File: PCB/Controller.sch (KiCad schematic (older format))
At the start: 15 parts, among them IC501 ATMEGA88-A, P501 PRG, SW501 Time Set, SW502 Alarm Set, SW503 Fast, SW504 Slow, SW505 Auto Time, SW506 Sleep, SW507 Summer Time, SW508 Alarm Enabled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

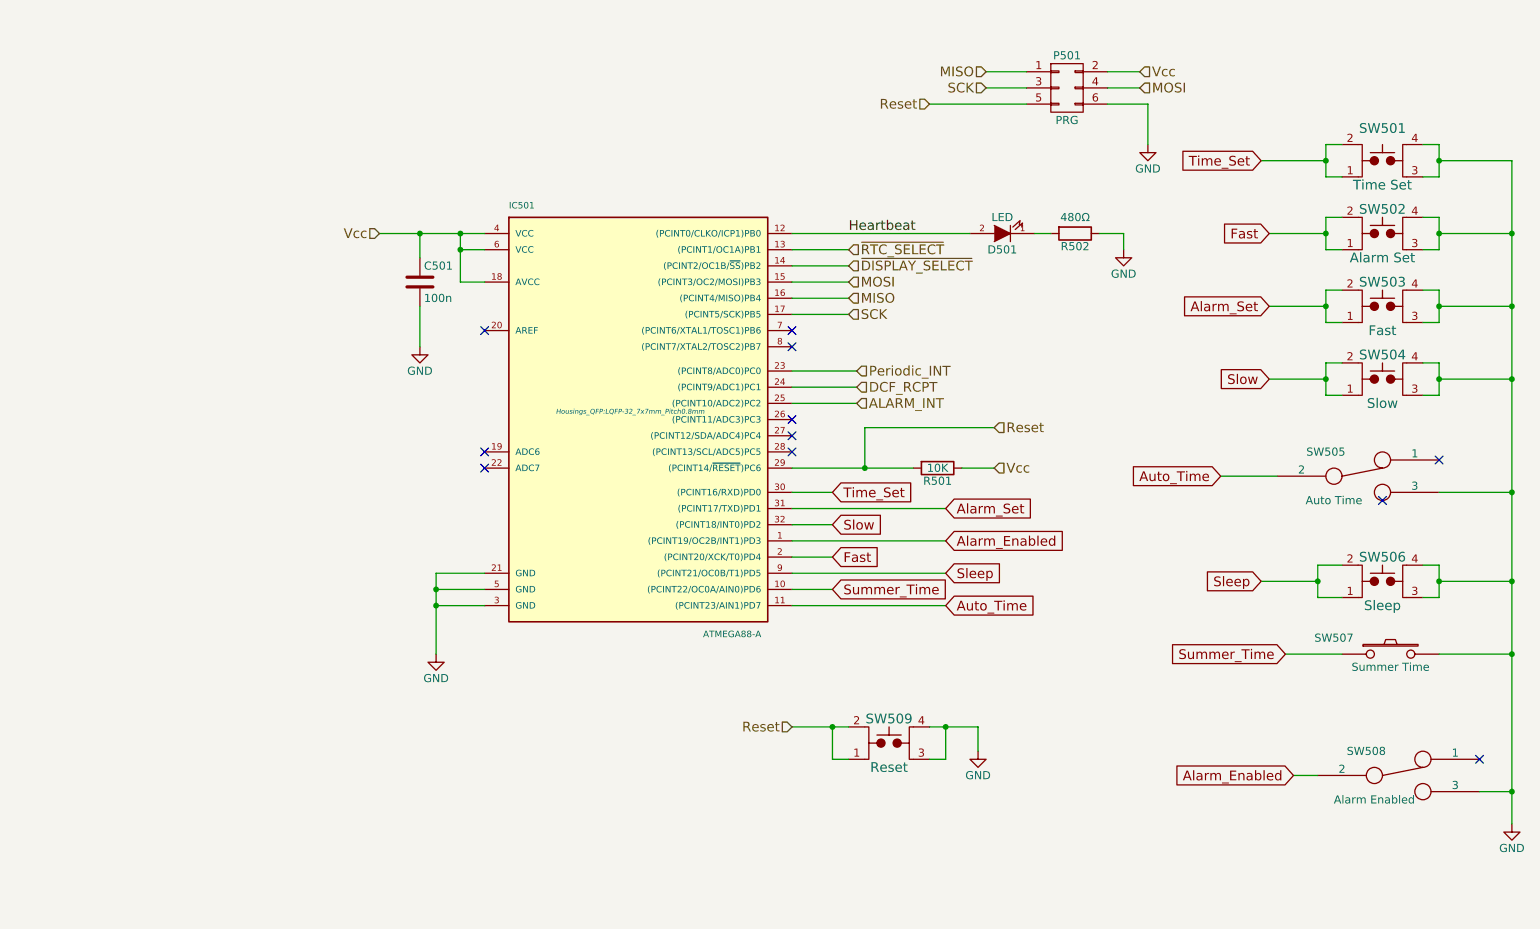
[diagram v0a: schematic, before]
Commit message: Added alarm
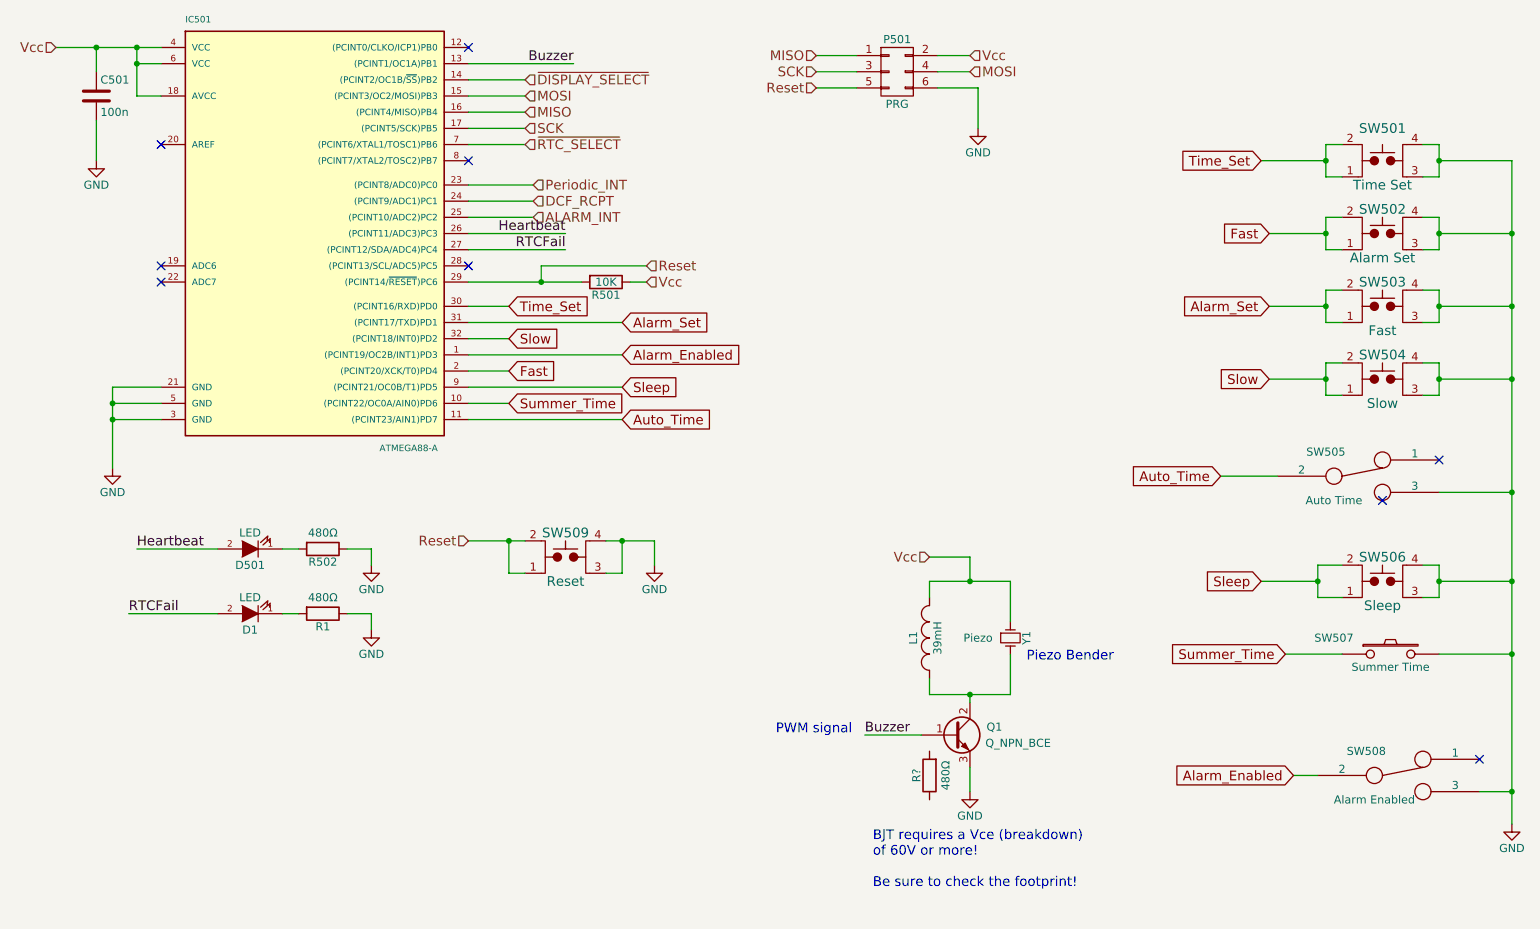
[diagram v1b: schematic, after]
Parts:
- added D1: LED, LEDs:LED-0805, symbol LED
- added L1: 39mH, symbol INDUCTOR_SMALL
- added Q1: Q_NPN_BCE, symbol Q_NPN_BCE
- added R1, R?: 480Ω, Resistors_SMD:R_0805_HandSoldering, symbol R
- added Y1: Piezo, symbol Crystal_Small
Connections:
- net GND: now also Q1.3 (E), R1.1
- net Heartbeat: now also IC501.26 ((PCINT11/ADC3)PC3); no longer IC501.12 ((PCINT0/CLKO/ICP1)PB0)
- net Vcc: now also L1.2, Y1.1
- net ~RTC_SELECT: now also IC501.7 ((PCINT6/XTAL1/TOSC1)PB6); no longer IC501.13 ((PCINT1/OC1A)PB1)
- net RTCFail: now reaches IC501.27 ((PCINT12/SDA/ADC4)PC4)
- net RTCFail: now also D1.2 (A)
- new net: D1.1 (K), R1.2
- new net: L1.1, Q1.2 (C), Y1.2
- new net Buzzer: IC501.13 ((PCINT1/OC1A)PB1), Q1.1 (B)
- no-connect marks 11 -> 9
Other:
- note added: "BJT requires a Vce (breakdown)\nof 60V or more!\n\nBe sure to check the footprint!"
- note added: "PWM signal"
- note added: "Piezo Bender"
- moved on the sheet: C501, D501, IC501, P501, R501, R502, SW509

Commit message: Re-organised the board to incorporate the MISO
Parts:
- removed D1: LED, LEDs:LED-0805, symbol LED
- removed L1: 39mH, symbol INDUCTOR_SMALL
- removed Q1: Q_NPN_BCE, symbol Q_NPN_BCE
- removed R1, R?: 480Ω, Resistors_SMD:R_0805_HandSoldering, symbol R
- removed SW505: Auto Time, tfac-footprints:AYZ0202AGRLC, symbol SWITCH_INV
- removed Y1: Piezo, symbol Crystal_Small
- added D503: 1N4148W, Diodes_SMD:SOD-123, symbol D
- added Q501: 2SD2391, TO_SOT_Packages_SMD:SOT89-3_Housing, symbol Q_NPN_BCE
- added SP501: CT-1205-SMT, tfac-footprints:CT-1205-SMT, symbol SPEAKER
- added SW505: AUTO_TIME, Pin_Headers:Pin_Header_Straight_1x02, symbol CONN_01X02
- D501: footprint LEDs:LED-0805 -> LEDs:LED_0805; ConradPN (none) -> Value; DigiKeyPN (none) -> Value; Link (none) -> Value; On-Hand (none) -> No; Voltage (none) -> Value
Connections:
- net Auto_Time: now also SW505.1 (P1)
- net Buzzer: now also Q501.1 (B)
- net GND: now also Q501.3 (E), SW505.2 (P2)
- net Vcc: now also D503.1 (K), SP501.1
- net RTCFail: no longer names the net of IC501.27 ((PCINT12/SDA/ADC4)PC4)
- new net: D503.2 (A), Q501.2 (C), SP501.2
- no-connect marks 9 -> 8
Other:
- note removed: "Piezo Bender"
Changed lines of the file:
@@
 Text GLabel 8600 3100 0    60   Input ~ 0
 Slow
-Text GLabel 8300 3700 0    60   Input ~ 0
+Text GLabel 8650 3600 0    60   Input ~ 0
 Auto_Time
 Text GLabel 8550 4350 0    60   Input ~ 0
@@
 U 1 1 55C107C5
 P 9350 4800
-F 0 "SW507" H 9000 4900 50  0000 C CNN
+F 0 "SW507" H 9000 4850 50  0000 C CNN
 F 1 "Summer Time" H 9350 4720 50  0000 C CNN
 F 2 "Pin_Headers:Pin_Header_Straight_1x02" H 9350 4800 60  0001 C CNN
@@
 $EndComp
 $Comp
-L SWITCH_INV SW505
-U 1 1 55D06426
-P 9150 3700
-F 0 "SW505" H 8950 3850 50  0000 C CNN
-F 1 "Auto Time" H 9000 3550 50  0000 C CNN
-F 2 "tfac-footprints:AYZ0202AGRLC" H 9150 3700 60  0001 C CNN
-F 3 "" H 9150 3700 60  0000 C CNN
-	1    9150 3700
-	1    0    0    -1
-$EndComp
-$Comp
 L SWITCH_INV SW508
 U 1 1 55D066FA
@@
 Wire Wire Line
 	10100 1750 10100 5850
-Connection ~ 10100 3800
 Wire Wire Line
 	8550 1750 8950 1750
@@
 Wire Wire Line
 	8600 3100 8950 3100
-Wire Wire Line
-	8300 3700 8650 3700
 Wire Wire Line
 	8550 4350 8900 4350
@@
 Connection ~ 10100 2650
 Connection ~ 9650 2650
-Wire Wire Line
-	9650 3800 10100 3800
-NoConn ~ 9650 3600
 Wire Wire Line
 	9050 3000 8950 3000
@@
 Connection ~ 9650 4350
 NoConn ~ 9900 5450
-NoConn ~ 9300 3850
 Wire Wire Line
 	1100 1050 1750 1050
@@
 F 0 "D501" H 2300 4250 50  0000 C CNN
 F 1 "LED" H 2300 4050 50  0000 C CNN
-F 2 "LEDs:LED-0805" H 2300 4150 60  0001 C CNN
+F 2 "LEDs:LED_0805" H 2300 4150 60  0001 C CNN
 F 3 "" H 2300 4150 60  0000 C CNN
+F 4 "Value" H 2300 4150 60  0001 C CNN "DigiKeyPN"
+F 5 "Value" H 2300 4150 60  0001 C CNN "Voltage"
+F 6 "Value" H 2300 4150 60  0001 C CNN "ConradPN"
+F 7 "Value" H 2300 4150 60  0001 C CNN "Link"
+F 8 "No" H 2300 4150 60  0001 C CNN "On-Hand"
 	1    2300 4150
 	-1   0    0    1
@@
 	4600 4300 4600 4100
 Connection ~ 4600 4100
-$Comp
-L LED D1
-U 1 1 56E1B9DB
-P 2300 4550
-F 0 "D1" H 2300 4650 50  0000 C CNN
-F 1 "LED" H 2300 4450 50  0000 C CNN
-F 2 "LEDs:LED-0805" H 2300 4550 60  0001 C CNN
-F 3 "" H 2300 4550 60  0000 C CNN
-	1    2300 4550
-	-1   0    0    1
-$EndComp
-$Comp
-L R R1
-U 1 1 56E1B9E1
-P 2750 4550
-F 0 "R1" V 2830 4550 50  0000 C CNN
-F 1 "480Ω" V 2650 4550 50  0000 C CNN
-F 2 "Resistors_SMD:R_0805_HandSoldering" V 2680 4550 30  0001 C CNN
-F 3 "" H 2750 4550 30  0000 C CNN
-	1    2750 4550
-	0    1    1    0
-$EndComp
-$Comp
-L GND #PWR016
-U 1 1 56E1B9E7
-P 3050 4650
-F 0 "#PWR016" H 3050 4400 50  0001 C CNN
-F 1 "GND" H 3050 4500 50  0000 C CNN
-F 2 "" H 3050 4650 60  0000 C CNN
-F 3 "" H 3050 4650 60  0000 C CNN
-	1    3050 4650
-	1    0    0    -1
-$EndComp
-Wire Wire Line
-	2500 4550 2600 4550
-Wire Wire Line
-	2900 4550 3050 4550
-Wire Wire Line
-	3050 4550 3050 4650
-Text Label 4250 2300 2    60   ~ 0
-RTCFail
-Wire Wire Line
-	2100 4550 1550 4550
-Text Label 1550 4550 0    60   ~ 0
-RTCFail
 Text Label 1600 4150 0    60   ~ 0
 Heartbeat
@@
 Wire Wire Line
 	3650 2200 4250 2200
-Wire Wire Line
-	3650 2300 4250 2300
 NoConn ~ 3650 1050
 NoConn ~ 3650 1750
 NoConn ~ 3650 2400
-$Comp
-L Crystal_Small Y1
-U 1 1 56E46684
-P 7000 4700
-F 0 "Y1" H 7000 4800 50  0000 C CNN
-F 1 "Piezo" V 7000 4500 50  0000 C CNN
-F 2 "" H 7000 4700 50  0000 C CNN
-F 3 "" H 7000 4700 50  0000 C CNN
-	1    7000 4700
-	0    1    1    0
-$EndComp
-$Comp
-L Q_NPN_BCE Q1
-U 1 1 56E4676D
-P 6650 5300
-F 0 "Q1" H 6950 5350 50  0000 R CNN
-F 1 "Q_NPN_BCE" H 7250 5250 50  0000 R CNN
-F 2 "" H 6850 5400 50  0000 C CNN
-F 3 "" H 6650 5300 50  0000 C CNN
-	1    6650 5300
-	1    0    0    -1
-$EndComp
-$Comp
-L INDUCTOR_SMALL L1
-U 1 1 56E46A19
-P 6500 4700
-F 0 "L1" H 6500 4800 50  0000 C CNN
-F 1 "39mH" H 6500 4650 50  0000 C CNN
-F 2 "" H 6500 4700 50  0000 C CNN
-F 3 "" H 6500 4700 50  0000 C CNN
-	1    6500 4700
-	0    -1   -1   0
-$EndComp
-Wire Wire Line
-	6500 4450 6500 4350
+Wire Wire Line
+	6500 4350 6500 4550
 Wire Wire Line
 	6500 4350 7000 4350
@@
 	7000 4350 7000 4600
 Wire Wire Line
-	6500 4950 6500 5050
+	6500 4850 6500 5050
 Wire Wire Line
 	6500 5050 7000 5050
@@
 	6750 4200 6500 4200
 Connection ~ 6750 4350
+Text Label 6100 5450 0    60   ~ 0
+Buzzer
+$Comp
+L GND #PWR016
+U 1 1 56E475A8
+P 6750 5800
+F 0 "#PWR016" H 6750 5550 50  0001 C CNN
+F 1 "GND" H 6750 5650 50  0000 C CNN
+F 2 "" H 6750 5800 60  0000 C CNN
+F 3 "" H 6750 5800 60  0000 C CNN
+	1    6750 5800
+	1    0    0    -1
+$EndComp
+Text Notes 5100 6400 0    60   ~ 0
+BJT requires a Vce (breakdown)\nof 60V or more!\n\nBe sure to check the footprint!
+Text Notes 5550 5450 0    60   ~ 0
+PWM signal
+Wire Wire Line
+	6450 5450 6100 5450
+Wire Wire Line
+	6750 5650 6750 5800
+Wire Wire Line
+	6750 5250 6750 5050
+Connection ~ 6750 5050
+$Comp
+L SPEAKER SP501
+U 1 1 5787E352
+P 7300 4700
+F 0 "SP501" H 7200 4950 50  0000 C CNN
+F 1 "CT-1205-SMT" H 7200 4450 50  0000 C CNN
+F 2 "tfac-footprints:CT-1205-SMT" H 7300 4700 50  0001 C CNN
+F 3 "http://www.cui.com/product/resource/ct-1205-smt.pdf" H 7300 4700 50  0001 C CNN
+F 4 "102-1199-2-ND" H 7300 4700 60  0001 C CNN "DigiKeyPN"
+F 5 "Value" H 7300 4700 60  0001 C CNN "Voltage"
+F 6 "Value" H 7300 4700 60  0001 C CNN "ConradPN"
+F 7 "Value" H 7300 4700 60  0001 C CNN "Link"
+F 8 "Yes" H 7300 4700 60  0001 C CNN "On-Hand"
+	1    7300 4700
+	1    0    0    -1
+$EndComp
+$Comp
+L D D503
+U 1 1 5787E3E5
+P 6500 4700
+F 0 "D503" H 6500 4800 50  0000 C CNN
+F 1 "1N4148W" H 6500 4600 50  0000 C CNN
+F 2 "Diodes_SMD:SOD-123" H 6500 4700 50  0001 C CNN
+F 3 "http://www.vishay.com/docs/85887/1n4148wfl-g.pdf" H 6500 4700 50  0001 C CNN
+F 4 "Value" H 6500 4700 60  0001 C CNN "DigiKeyPN"
+F 5 "Value" H 6500 4700 60  0001 C CNN "Voltage"
+F 6 "Value" H 6500 4700 60  0001 C CNN "ConradPN"
+F 7 "Value" H 6500 4700 60  0001 C CNN "Link"
+F 8 "Yes" H 6500 4700 60  0001 C CNN "On-Hand"
+F 9 "Value" H 6500 4700 60  0001 C CNN " 1N4148WFL-G3-08GICT-ND "
+	1    6500 4700
+	0    1    1    0
+$EndComp
+$Comp
+L Q_NPN_BCE Q501
+U 1 1 5787E5A8
+P 6650 5450
+F 0 "Q501" H 7100 5500 50  0000 R CNN
+F 1 "2SD2391" H 7250 5400 50  0000 R CNN
+F 2 "TO_SOT_Packages_SMD:SOT89-3_Housing" H 6850 5550 50  0001 C CNN
+F 3 "http://rohmfs.rohm.com/en/products/databook/datasheet/discrete/transistor/bipolar/2sd2391t100q-e.pdf" H 6650 5450 50  0001 C CNN
+F 4 "Value" H 6650 5450 60  0001 C CNN "DigiKeyPN"
+F 5 "Value" H 6650 5450 60  0001 C CNN "Voltage"
+F 6 "Value" H 6650 5450 60  0001 C CNN "ConradPN"
+F 7 "Value" H 6650 5450 60  0001 C CNN "Link"
+F 8 "Yes" H 6650 5450 60  0001 C CNN "On-Hand"
+	1    6650 5450
+	1    0    0    -1
+$EndComp
+NoConn ~ 3650 2300
 Text HLabel 6500 4200 0    60   Input ~ 0
 Vcc
-Wire Wire Line
-	6750 5100 6750 5050
-Connection ~ 6750 5050
-Wire Wire Line
-	6450 5300 6100 5300
-Text Label 6100 5300 0    60   ~ 0
-Buzzer
+$Comp
+L CONN_01X02 SW505
+U 1 1 579AA172
+P 9300 3650
+F 0 "SW505" H 9300 3800 50  0000 C CNN
+F 1 "AUTO_TIME" H 9250 3450 50  0000 C CNN
+F 2 "Pin_Headers:Pin_Header_Straight_1x02" H 9300 3650 50  0001 C CNN
+F 3 "" H 9300 3650 50  0000 C CNN
+	1    9300 3650
+	1    0    0    -1
+$EndComp
+Wire Wire Line
+	8650 3600 9100 3600
 $Comp
 L GND #PWR017
-U 1 1 56E475A8
-P 6750 5650
-F 0 "#PWR017" H 6750 5400 50  0001 C CNN
-F 1 "GND" H 6750 5500 50  0000 C CNN
-F 2 "" H 6750 5650 60  0000 C CNN
-F 3 "" H 6750 5650 60  0000 C CNN
-	1    6750 5650
-	1    0    0    -1
-$EndComp
-Wire Wire Line
-	6750 5500 6750 5650
-Text Notes 6150 6250 0    60   ~ 0
-BJT requires a Vce (breakdown)\nof 60V or more!\n\nBe sure to check the footprint!
-Text Notes 7100 4850 0    60   ~ 0
-Piezo Bender
-Text Notes 5550 5300 0    60   ~ 0
-PWM signal
-$Comp
-L R R?
-U 1 1 56E98D80
-P 6500 5550
-F 0 "R?" V 6580 5550 50  0000 C CNN
-F 1 "480Ω" V 6400 5550 50  0000 C CNN
-F 2 "Resistors_SMD:R_0805_HandSoldering" V 6430 5550 30  0001 C CNN
-F 3 "" H 6500 5550 30  0000 C CNN
-	1    6500 5550
-	-1   0    0    1
-$EndComp
+U 1 1 579AA3CB
+P 8900 3850
+F 0 "#PWR017" H 8900 3600 50  0001 C CNN
+F 1 "GND" H 8900 3700 50  0000 C CNN
+F 2 "" H 8900 3850 60  0000 C CNN
+F 3 "" H 8900 3850 60  0000 C CNN
+	1    8900 3850
+	1    0    0    -1
+$EndComp
+Wire Wire Line
+	9100 3700 8900 3700
+Wire Wire Line
+	8900 3700 8900 3850
 $EndSCHEMATC
